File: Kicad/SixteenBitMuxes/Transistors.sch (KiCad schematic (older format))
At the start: 20 parts, among them Q1 PN2222A, Q10 2SC1815, Q12 S9013, Q14 S9018, Q15 BC848B, Q16 2SC1623, Q17 MPSA18, Q19 2N5088, Q2 MMBT3904, Q3 MMBT5551L, Q4 MMBTA42, Q5 BC807, Q6 BC846, Q7 BC847B, Q8 BC847C, Q9 C945, U8 CD4067BM, U9 CD4067BM

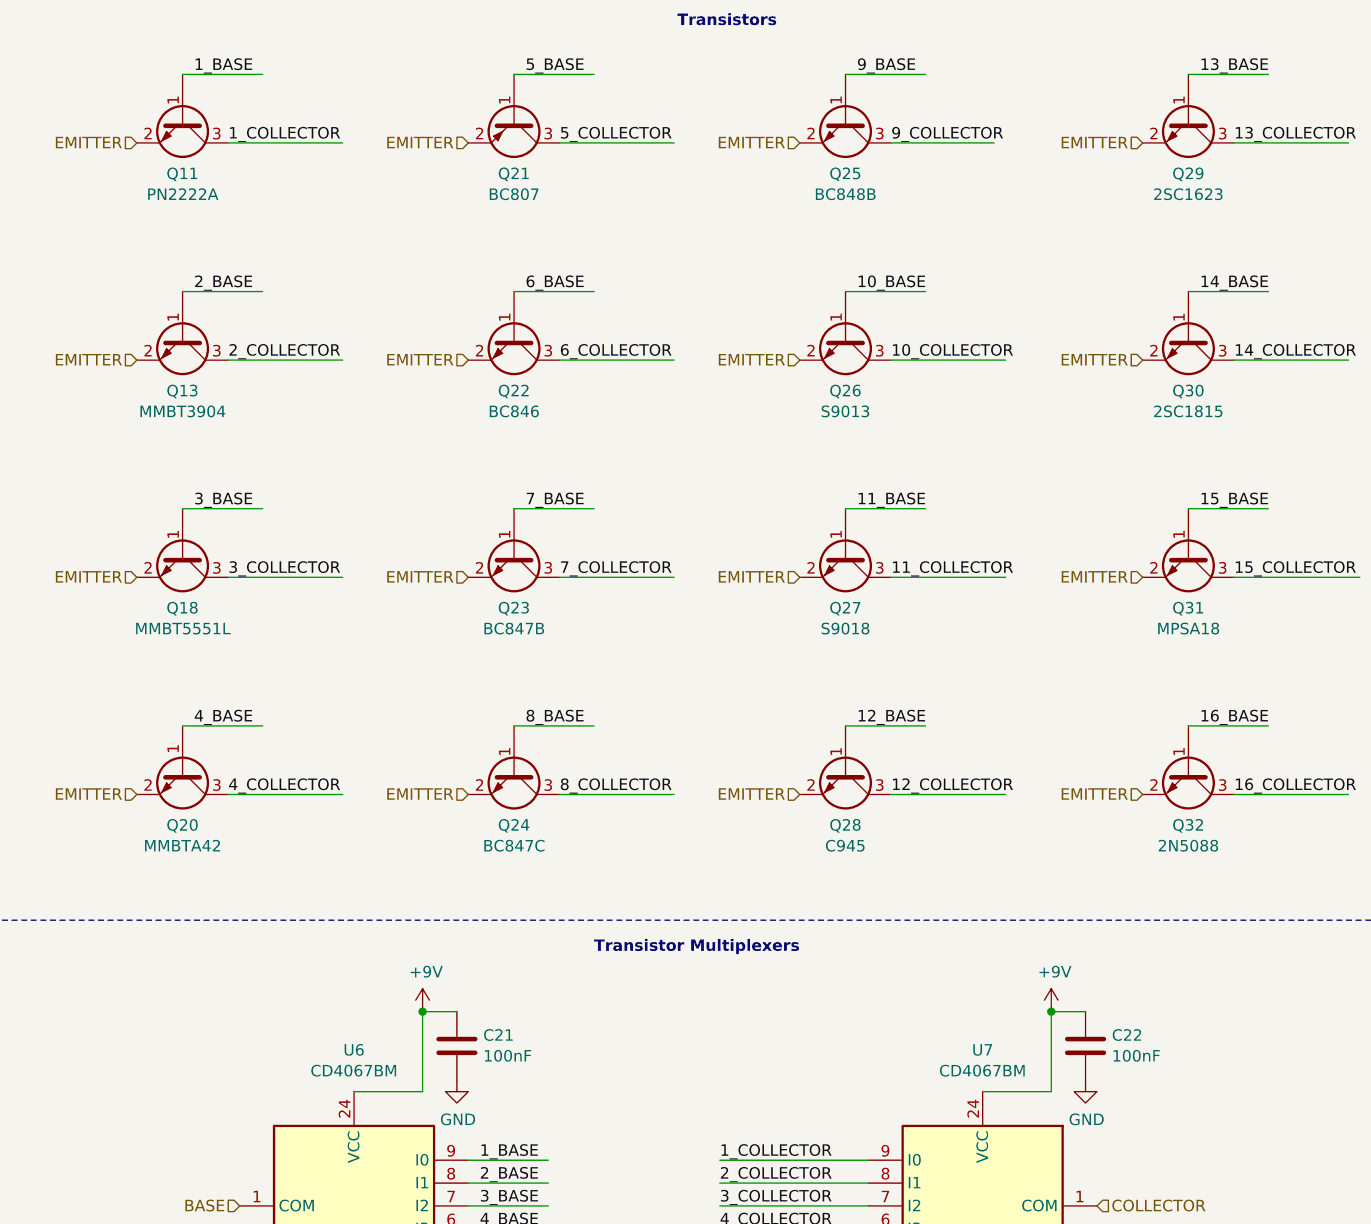
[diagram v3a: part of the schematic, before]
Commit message: Code + resistors
Many code changes (UI) + resistors -> pulldowns.
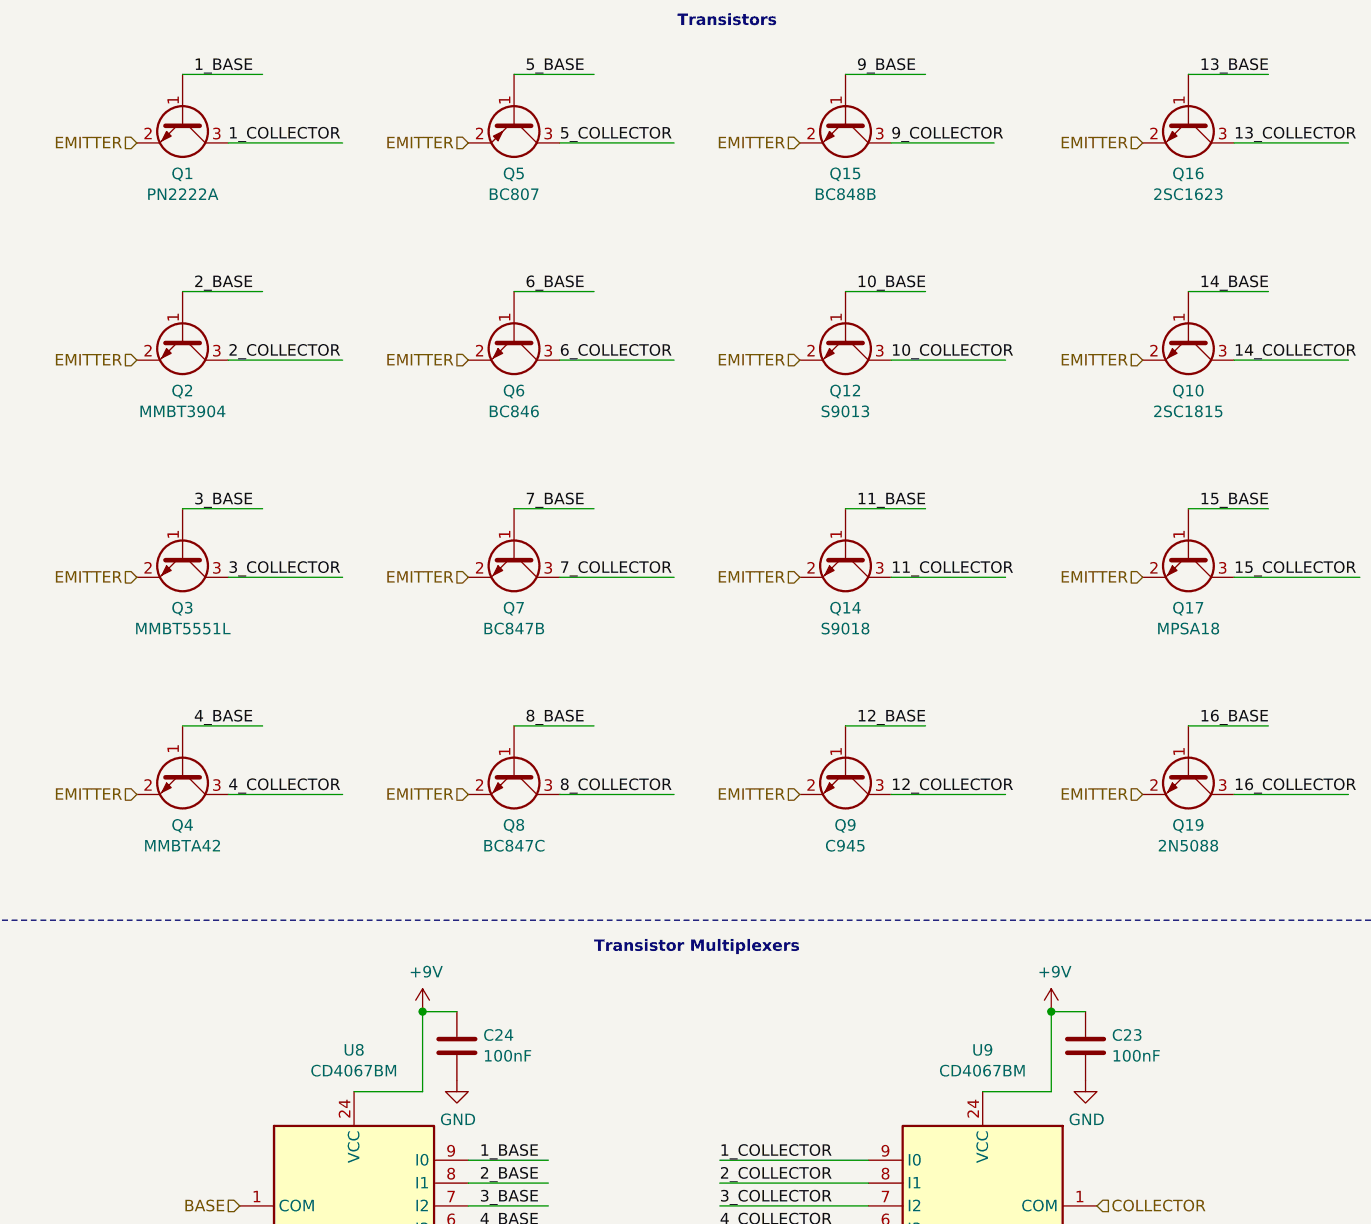
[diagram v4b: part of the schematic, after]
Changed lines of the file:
@@
 $Descr A4 11693 8268
 encoding utf-8
-Sheet 6 9
+Sheet 7 9
 Title "Guitar Pedal Effect Fuzz Digitally Controlled"
 Date "2020-04-07"
@@
 AR Path="/5F9746B8/5EA993A8" Ref="Q24"  Part="1"
 AR Path="/5ED1AB26/5EA993A8" Ref="Q20"  Part="1"
-F 0 "Q20" V 1735 4000 50  0000 C CNN
+F 0 "Q4" V 1735 4000 50  0000 C CNN
 F 1 "MMBTA42" V 1826 4000 50  0000 C CNN
 F 2 "Package_TO_SOT_SMD:SOT-23_Handsoldering" H 1700 3925 50  0001 L CIN
@@
 AR Path="/5F9746B8/5EA993B4" Ref="Q39"  Part="1"
 AR Path="/5ED1AB26/5EA993B4" Ref="Q32"  Part="1"
-F 0 "Q32" V 6135 4000 50  0000 C CNN
+F 0 "Q19" V 6135 4000 50  0000 C CNN
 F 1 "2N5088" V 6226 4000 50  0000 C CNN
 F 2 "Package_TO_SOT_THT:TO-92_Inline" H 6100 3925 50  0001 L CIN
@@
 AR Path="/5F9746B8/5EA993C0" Ref="Q37"  Part="1"
 AR Path="/5ED1AB26/5EA993C0" Ref="Q31"  Part="1"
-F 0 "Q31" V 6135 3050 50  0000 C CNN
+F 0 "Q17" V 6135 3050 50  0000 C CNN
 F 1 "MPSA18" V 6226 3050 50  0000 C CNN
 F 2 "Package_TO_SOT_THT:TO-92_Inline" H 6100 2975 50  0001 L CIN
@@
 AR Path="/5F9746B8/5EA993CD" Ref="Q36"  Part="1"
 AR Path="/5ED1AB26/5EA993CD" Ref="Q29"  Part="1"
-F 0 "Q29" V 6135 1150 50  0000 C CNN
+F 0 "Q16" V 6135 1150 50  0000 C CNN
 F 1 "2SC1623" V 6226 1150 50  0000 C CNN
 F 2 "Package_TO_SOT_SMD:SOT-23_Handsoldering" H 6100 1250 50  0001 C CNN
@@
 AR Path="/5F9746B8/5EA993FC" Ref="Q28"  Part="1"
 AR Path="/5ED1AB26/5EA993FC" Ref="Q24"  Part="1"
-F 0 "Q24" V 3185 4000 50  0000 C CNN
+F 0 "Q8" V 3185 4000 50  0000 C CNN
 F 1 "BC847C" V 3276 4000 50  0000 C CNN
 F 2 "Package_TO_SOT_SMD:SOT-23_Handsoldering" H 3150 3925 50  0001 L CIN
@@
 AR Path="/5F9746B8/5EA99402" Ref="Q27"  Part="1"
 AR Path="/5ED1AB26/5EA99402" Ref="Q23"  Part="1"
-F 0 "Q23" V 3185 3050 50  0000 C CNN
+F 0 "Q7" V 3185 3050 50  0000 C CNN
 F 1 "BC847B" V 3276 3050 50  0000 C CNN
 F 2 "Package_TO_SOT_SMD:SOT-23_Handsoldering" H 3150 3150 50  0001 C CNN
@@
 AR Path="/5F9746B8/5EA99408" Ref="Q26"  Part="1"
 AR Path="/5ED1AB26/5EA99408" Ref="Q22"  Part="1"
-F 0 "Q22" V 3185 2100 50  0000 C CNN
+F 0 "Q6" V 3185 2100 50  0000 C CNN
 F 1 "BC846" V 3276 2100 50  0000 C CNN
 F 2 "Package_TO_SOT_SMD:SOT-23_Handsoldering" H 3150 2025 50  0001 L CIN
@@
 AR Path="/5F9746B8/5EA9940E" Ref="Q25"  Part="1"
 AR Path="/5ED1AB26/5EA9940E" Ref="Q21"  Part="1"
-F 0 "Q21" V 3185 1150 50  0000 C CNN
+F 0 "Q5" V 3185 1150 50  0000 C CNN
 F 1 "BC807" V 3276 1150 50  0000 C CNN
 F 2 "Package_TO_SOT_SMD:SOT-23_Handsoldering" H 3150 1075 50  0001 L CIN
@@
 AR Path="/5F9746B8/5EA99637" Ref="Q23"  Part="1"
 AR Path="/5ED1AB26/5EA99637" Ref="Q18"  Part="1"
-F 0 "Q18" V 1735 3050 50  0000 C CNN
+F 0 "Q3" V 1735 3050 50  0000 C CNN
 F 1 "MMBT5551L" V 1826 3050 50  0000 C CNN
 F 2 "Package_TO_SOT_SMD:SOT-23_Handsoldering" H 1700 2975 50  0001 L CIN
@@
 AR Path="/5F9746B8/5EA99643" Ref="Q22"  Part="1"
 AR Path="/5ED1AB26/5EA99643" Ref="Q13"  Part="1"
-F 0 "Q13" V 1735 2100 50  0000 C CNN
+F 0 "Q2" V 1735 2100 50  0000 C CNN
 F 1 "MMBT3904" V 1826 2100 50  0000 C CNN
 F 2 "Package_TO_SOT_SMD:SOT-23_Handsoldering" H 1700 2025 50  0001 L CIN
@@
 AR Path="/5F9746B8/5F014460" Ref="Q30"  Part="1"
 AR Path="/5ED1AB26/5F014460" Ref="Q30"  Part="1"
-F 0 "Q30" V 6135 2100 50  0000 C CNN
+F 0 "Q10" V 6135 2100 50  0000 C CNN
 F 1 "2SC1815" V 6226 2100 50  0000 C CNN
 F 2 "Package_TO_SOT_SMD:SOT-23_Handsoldering" H 6100 2025 50  0001 L CIN
@@
 AR Path="/5F9746B8/5F02F005" Ref="Q29"  Part="1"
 AR Path="/5ED1AB26/5F02F005" Ref="Q28"  Part="1"
-F 0 "Q28" V 4635 4000 50  0000 C CNN
+F 0 "Q9" V 4635 4000 50  0000 C CNN
 F 1 "C945" V 4726 4000 50  0000 C CNN
 F 2 "Package_TO_SOT_SMD:SOT-23_Handsoldering" H 4600 4100 50  0001 C CNN
@@
 AR Path="/5F9746B8/5EA9963D" Ref="Q21"  Part="1"
 AR Path="/5ED1AB26/5EA9963D" Ref="Q11"  Part="1"
-F 0 "Q11" V 1735 1150 50  0000 C CNN
+F 0 "Q1" V 1735 1150 50  0000 C CNN
 F 1 "PN2222A" V 1826 1150 50  0000 C CNN
 F 2 "Package_TO_SOT_SMD:SOT-23_Handsoldering" H 1700 1075 50  0001 L CIN
@@
 AR Path="/5F9746B8/5EA993C7" Ref="Q35"  Part="1"
 AR Path="/5ED1AB26/5EA993C7" Ref="Q25"  Part="1"
-F 0 "Q25" V 4635 1150 50  0000 C CNN
+F 0 "Q15" V 4635 1150 50  0000 C CNN
 F 1 "BC848B" V 4726 1150 50  0000 C CNN
 F 2 "Package_TO_SOT_SMD:SOT-23_Handsoldering" H 4600 1075 50  0001 L CIN
@@
 AR Path="/5F9746B8/5EA993D3" Ref="Q34"  Part="1"
 AR Path="/5ED1AB26/5EA993D3" Ref="Q27"  Part="1"
-F 0 "Q27" V 4635 3050 50  0000 C CNN
+F 0 "Q14" V 4635 3050 50  0000 C CNN
 F 1 "S9018" V 4726 3050 50  0000 C CNN
 F 2 "Package_TO_SOT_SMD:SOT-23_Handsoldering" H 4600 3150 50  0001 C CNN
@@
 AR Path="/5F9746B8/5EA993DF" Ref="Q32"  Part="1"
 AR Path="/5ED1AB26/5EA993DF" Ref="Q26"  Part="1"
-F 0 "Q26" V 4635 2100 50  0000 C CNN
+F 0 "Q12" V 4635 2100 50  0000 C CNN
 F 1 "S9013" V 4726 2100 50  0000 C CNN
 F 2 "Package_TO_SOT_SMD:SOT-23_Handsoldering" H 4600 2200 50  0001 C CNN
@@
 AR Path="/5E9AE796/5EA4E538" Ref="U9"  Part="1"
 AR Path="/5ED1AB26/5EA4E538" Ref="U7"  Part="1"
-F 0 "U7" H 5000 7581 50  0000 C CNN
+F 0 "U9" H 5000 7581 50  0000 C CNN
 F 1 "CD4067BM" H 5000 7490 50  0000 C CNN
 F 2 "Package_SO:SOIC-24W_7.5x15.4mm_P1.27mm" H 5900 5400 50  0001 C CIN
@@
 AR Path="/5E9AE796/5EA3E429" Ref="U8"  Part="1"
 AR Path="/5ED1AB26/5EA3E429" Ref="U6"  Part="1"
-F 0 "U6" H 2250 7581 50  0000 C CNN
+F 0 "U8" H 2250 7581 50  0000 C CNN
 F 1 "CD4067BM" H 2250 7490 50  0000 C CNN
 F 2 "Package_SO:SOIC-24W_7.5x15.4mm_P1.27mm" H 3150 5400 50  0001 C CIN
@@
 AR Path="/5F9746B8/5EA99533" Ref="C31"  Part="1"
 AR Path="/5ED1AB26/5EA99533" Ref="C21"  Part="1"
-F 0 "C21" H 2815 5246 50  0000 L CNN
+F 0 "C24" H 2815 5246 50  0000 L CNN
 F 1 "100nF" H 2815 5155 50  0000 L CNN
 F 2 "Capacitor_SMD:C_0805_2012Metric_Pad1.15x1.40mm_HandSolder" H 2738 5050 50  0001 C CNN
@@
 AR Path="/5F9746B8/5ECDF6D6" Ref="C?"  Part="1"
 AR Path="/5ED1AB26/5ECDF6D6" Ref="C22"  Part="1"
-F 0 "C22" H 5565 5246 50  0000 L CNN
+F 0 "C23" H 5565 5246 50  0000 L CNN
 F 1 "100nF" H 5565 5155 50  0000 L CNN
 F 2 "Capacitor_SMD:C_0805_2012Metric_Pad1.15x1.40mm_HandSolder" H 5488 5050 50  0001 C CNN

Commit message: Improvements according video youtube
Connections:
- net labels added: +9V_SAFE
- net labels removed: +9V
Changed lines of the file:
@@
 AR Path="/5E9AE796/5EA4E538" Ref="U9"  Part="1"
 AR Path="/5ED1AB26/5EA4E538" Ref="U7"  Part="1"
-F 0 "U9" H 5000 7581 50  0000 C CNN
-F 1 "CD4067BM" H 5000 7490 50  0000 C CNN
+F 0 "U9" H 5400 7450 50  0000 C CNN
+F 1 "CD4067BM" H 5450 7350 50  0000 C CNN
 F 2 "Package_SO:SOIC-24W_7.5x15.4mm_P1.27mm" H 5900 5400 50  0001 C CIN
 F 3 "http://www.ti.com/lit/ds/symlink/cd74hc4067.pdf" H 4650 7250 50  0001 C CNN
@@
 AR Path="/5E9AE796/5EA3E429" Ref="U8"  Part="1"
 AR Path="/5ED1AB26/5EA3E429" Ref="U6"  Part="1"
-F 0 "U8" H 2250 7581 50  0000 C CNN
-F 1 "CD4067BM" H 2250 7490 50  0000 C CNN
+F 0 "U8" H 1850 7450 50  0000 C CNN
+F 1 "CD4067BM" H 1800 7350 50  0000 C CNN
 F 2 "Package_SO:SOIC-24W_7.5x15.4mm_P1.27mm" H 3150 5400 50  0001 C CIN
 F 3 "http://www.ti.com/lit/ds/symlink/cd74hc4067.pdf" H 1900 7250 50  0001 C CNN
 	1    2250 6400
-	1    0    0    -1
-$EndComp
-$Comp
-L power:+9V #PWR0144
-U 1 1 5EAD9CE0
-P 2550 5050
-AR Path="/5E9AE796/5EAD9CE0" Ref="#PWR0144"  Part="1"
-AR Path="/5F9746B8/5EAD9CE0" Ref="#PWR0129"  Part="1"
-AR Path="/5ED1AB26/5EAD9CE0" Ref="#PWR0109"  Part="1"
-F 0 "#PWR0144" H 2550 4900 50  0001 C CNN
-F 1 "+9V" H 2565 5223 50  0000 C CNN
-F 2 "" H 2550 5050 50  0001 C CNN
-F 3 "" H 2550 5050 50  0001 C CNN
-	1    2550 5050
 	1    0    0    -1
 $EndComp
@@
 Wire Wire Line
 	2550 5050 2550 5400
-Connection ~ 2550 5050
 Wire Wire Line
 	2550 5400 2250 5400
@@
 Transistor Multiplexers\n
 $Comp
-L power:+9V #PWR0133
-U 1 1 5ECDD1BA
-P 5300 5050
-AR Path="/5E9AE796/5ECDD1BA" Ref="#PWR0133"  Part="1"
-AR Path="/5F9746B8/5ECDD1BA" Ref="#PWR?"  Part="1"
-AR Path="/5ED1AB26/5ECDD1BA" Ref="#PWR0121"  Part="1"
-F 0 "#PWR0133" H 5300 4900 50  0001 C CNN
-F 1 "+9V" H 5315 5223 50  0000 C CNN
-F 2 "" H 5300 5050 50  0001 C CNN
-F 3 "" H 5300 5050 50  0001 C CNN
-	1    5300 5050
-	1    0    0    -1
-$EndComp
-$Comp
 L Device:C C?
 U 1 1 5ECDF6D6
@@
 Wire Wire Line
 	5300 5400 5300 5050
-Connection ~ 5300 5050
 Wire Wire Line
 	5300 5400 5000 5400
@@
 	1    0    0    -1
 $EndComp
+Text HLabel 2250 5400 1    50   Input ~ 0
++9V_SAFE
+Text HLabel 5000 5400 1    50   Input ~ 0
++9V_SAFE
 $EndSCHEMATC
